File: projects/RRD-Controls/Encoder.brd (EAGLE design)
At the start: 20.3 x 35.6 mm, 3 parts

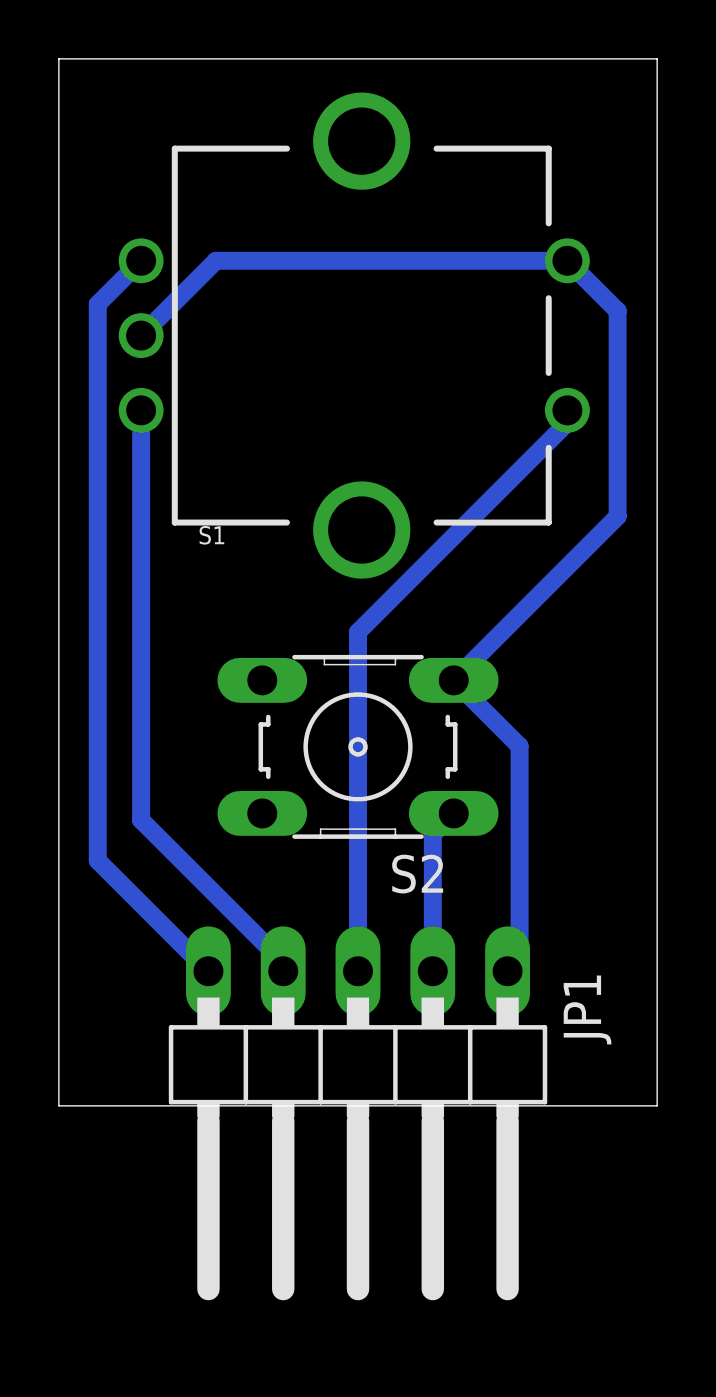
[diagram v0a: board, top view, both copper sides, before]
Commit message: New 32-bit AMR3350 (probably will be renamed), + other edits
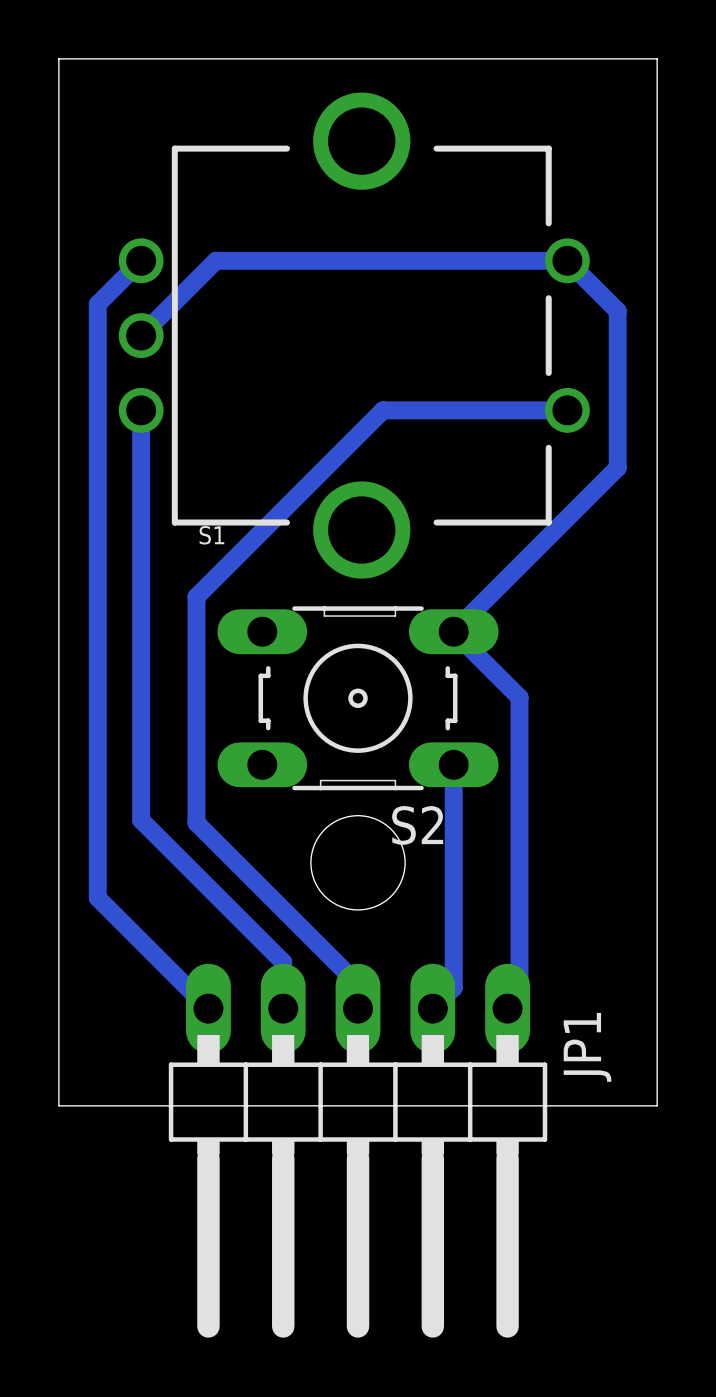
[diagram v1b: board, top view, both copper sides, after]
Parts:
- moved S2 1.65 mm to (10.2, 13.8)
- moved JP1 1.27 mm to (10.2, -0.51)
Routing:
- net ENC_SW: track 22.0 -> 31.5 mm
- net RESET: track 5.65 -> 8.57 mm
- net GND: track 43.8 -> 45.0 mm
- net ENC_B: track 21.0 -> 22.3 mm
- net ENC_A: track 26.3 -> 27.6 mm
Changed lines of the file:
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@@
 <setting verticaltext="up"/>
 </settings>
-<grid distance="50" unitdist="mil" unit="mil" style="dots" multiple="1" display="yes" altdistance="5" altunitdist="mil" altunit="mil"/>
+<grid distance="50" unitdist="mil" unit="mm" style="dots" multiple="1" display="yes" altdistance="5" altunitdist="mil" altunit="mil"/>
 <layers>
 <layer number="1" name="Top" color="4" fill="1" visible="yes" active="yes"/>
@@
 <layer number="43" name="vRestrict" color="2" fill="10" visible="yes" active="yes"/>
 <layer number="44" name="Drills" color="7" fill="1" visible="no" active="yes"/>
-<layer number="45" name="Holes" color="7" fill="1" visible="no" active="yes"/>
+<layer number="45" name="Holes" color="7" fill="1" visible="yes" active="yes"/>
 <layer number="46" name="Milling" color="3" fill="1" visible="no" active="yes"/>
 <layer number="47" name="Measures" color="7" fill="1" visible="no" active="yes"/>
@@
 </layers>
 <board>
+<fusionsync huburn="a.cGVyc29uYWw6dWUyYWY5YmU0" projecturn="a.cGVyc29uYWw6dWUyYWY5YmU0IzIwMTgwNTA2MTMwNzk4NzU2" f3durn="urn:adsk.wipprod:dm.lineage:ghSnY2K8RTWHbbuxzUc_hQ" pcbguid="3d89ad0b-1789-465d-8edf-d24fb5f6a05f" lastpulledtime="" lastsyncedchangeguid="ebffb4b7-4351-7158-2c67-7c1263c4be28"/>
 <plain>
 <wire x1="0" y1="0" x2="20.32" y2="0" width="0" layer="20"/>
@@
 <wire x1="20.32" y1="35.56" x2="0" y2="35.56" width="0" layer="20"/>
 <wire x1="0" y1="35.56" x2="0" y2="0" width="0" layer="20"/>
+<hole x="10.16" y="8.255" drill="3.2"/>
 </plain>
 <attributes>
@@
 </autorouter>
 <elements>
-<element name="JP1" library="pinhead" library_urn="urn:adsk.eagle:library:325" package="1X05/90" package3d_urn="urn:adsk.eagle:package:22467/2" value="" x="10.16" y="0.762" smashed="yes" rot="R180">
-<attribute name="NAME" x="17.145" y="4.572" size="1.27" layer="25" ratio="10" rot="R270"/>
-<attribute name="VALUE" x="1.905" y="4.572" size="1.27" layer="27" rot="R270"/>
+<element name="JP1" library="pinhead" library_urn="urn:adsk.eagle:library:325" package="1X05/90" package3d_urn="urn:adsk.eagle:package:22467/2" value="" x="10.16" y="-0.508" smashed="yes" rot="R180">
+<attribute name="NAME" x="17.145" y="3.302" size="1.27" layer="25" ratio="10" rot="R270"/>
+<attribute name="VALUE" x="1.905" y="3.302" size="1.27" layer="27" rot="R270"/>
 </element>
 <element name="S1" library="SparkFun-Switches" library_urn="urn:adsk.eagle:library:535" package="ROTARY_ENC_PLAIN" package3d_urn="urn:adsk.eagle:package:40158/1" value="ENCODER-SWITCH" x="10.287" y="26.162" smashed="yes" rot="R180">
@@
 <attribute name="VALUE" x="5.207" y="32.639" size="0.6096" layer="27" font="vector" ratio="20" rot="R180" align="top-center"/>
 </element>
-<element name="S2" library="switch-omron" library_urn="urn:adsk.eagle:library:377" package="B3F-10XX" package3d_urn="urn:adsk.eagle:package:27496/1" value="" x="10.16" y="12.192" smashed="yes" rot="R180">
-<attribute name="MF" value="" x="-7.62" y="46.482" size="1.778" layer="27" rot="R180" display="off"/>
-<attribute name="MPN" value="B3F-1000" x="-7.62" y="46.482" size="1.778" layer="27" rot="R180" display="off"/>
-<attribute name="NAME" x="13.208" y="8.509" size="1.27" layer="25" ratio="10" rot="R180"/>
-<attribute name="OC_FARNELL" value="176432" x="-7.62" y="46.482" size="1.778" layer="27" rot="R180" display="off"/>
-<attribute name="OC_NEWARK" value="36M3542" x="-7.62" y="46.482" size="1.778" layer="27" rot="R180" display="off"/>
-<attribute name="VALUE" x="13.208" y="17.272" size="1.27" layer="27" ratio="10" rot="R180"/>
+<element name="S2" library="switch-omron" library_urn="urn:adsk.eagle:library:377" package="B3F-10XX" package3d_urn="urn:adsk.eagle:package:27496/1" value="" x="10.16" y="13.843" smashed="yes" rot="R180">
+<attribute name="MF" value="" x="-7.62" y="48.133" size="1.778" layer="27" rot="R180" display="off"/>
+<attribute name="MPN" value="B3F-1000" x="-7.62" y="48.133" size="1.778" layer="27" rot="R180" display="off"/>
+<attribute name="NAME" x="13.208" y="10.16" size="1.27" layer="25" ratio="10" rot="R180"/>
+<attribute name="OC_FARNELL" value="176432" x="-7.62" y="48.133" size="1.778" layer="27" rot="R180" display="off"/>
+<attribute name="OC_NEWARK" value="36M3542" x="-7.62" y="48.133" size="1.778" layer="27" rot="R180" display="off"/>
+<attribute name="VALUE" x="13.208" y="18.923" size="1.27" layer="27" ratio="10" rot="R180"/>
 </element>
 </elements>
@@
 <wire x1="2.794" y1="26.162" x2="5.334" y2="28.702" width="0.6096" layer="16"/>
 <wire x1="17.272" y1="28.702" x2="18.9792" y2="26.9948" width="0.6096" layer="16"/>
-<wire x1="18.9792" y1="20.0206" x2="13.4112" y2="14.4526" width="0.6096" layer="16"/>
-<wire x1="18.9792" y1="26.9948" x2="18.9792" y2="20.0206" width="0.6096" layer="16"/>
-<wire x1="15.6464" y1="12.2174" x2="15.6464" y2="4.9784" width="0.6096" layer="16"/>
-<wire x1="15.6464" y1="4.9784" x2="15.24" y2="4.572" width="0.6096" layer="16"/>
-<wire x1="13.4112" y1="14.4526" x2="15.6464" y2="12.2174" width="0.6096" layer="16"/>
+<wire x1="18.9792" y1="21.6716" x2="13.4112" y2="16.1036" width="0.6096" layer="16"/>
+<wire x1="18.9792" y1="26.9948" x2="18.9792" y2="21.6716" width="0.6096" layer="16"/>
+<wire x1="15.6464" y1="13.8684" x2="15.6464" y2="3.7084" width="0.6096" layer="16"/>
+<wire x1="15.6464" y1="3.7084" x2="15.24" y2="3.302" width="0.6096" layer="16"/>
+<wire x1="13.4112" y1="16.1036" x2="15.6464" y2="13.8684" width="0.6096" layer="16"/>
 </signal>
 <signal name="RESET">
 <contactref element="S2" pad="1"/>
 <contactref element="JP1" pad="2"/>
-<wire x1="12.7" y1="4.572" x2="12.7" y2="9.2202" width="0.6096" layer="16"/>
-<wire x1="12.7" y1="9.2202" x2="13.4112" y2="9.9314" width="0.6096" layer="16"/>
+<wire x1="13.4112" y1="11.5824" x2="13.4112" y2="4.0132" width="0.6096" layer="16"/>
+<wire x1="13.4112" y1="4.0132" x2="12.7" y2="3.302" width="0.6096" layer="16"/>
 </signal>
 <signal name="ENC_A">
@@
 <contactref element="JP1" pad="5"/>
 <wire x1="2.794" y1="28.702" x2="1.3208" y2="27.2288" width="0.6096" layer="16"/>
-<wire x1="1.3208" y1="8.3312" x2="5.08" y2="4.572" width="0.6096" layer="16"/>
-<wire x1="1.3208" y1="27.2288" x2="1.3208" y2="8.3312" width="0.6096" layer="16"/>
+<wire x1="1.3208" y1="7.0612" x2="5.08" y2="3.302" width="0.6096" layer="16"/>
+<wire x1="1.3208" y1="27.2288" x2="1.3208" y2="7.0612" width="0.6096" layer="16"/>
 </signal>
 <signal name="ENC_B">
@@
 <contactref element="JP1" pad="4"/>
 <wire x1="2.794" y1="23.622" x2="2.794" y2="9.703425" width="0.6096" layer="16"/>
-<wire x1="7.62" y1="4.572" x2="7.62" y2="4.877425" width="0.6096" layer="16"/>
+<wire x1="7.62" y1="3.302" x2="7.62" y2="4.877425" width="0.6096" layer="16"/>
 <wire x1="7.62" y1="4.877425" x2="2.794" y2="9.703425" width="0.6096" layer="16"/>
 </signal>
@@
 <contactref element="S1" pad="SW+"/>
 <contactref element="JP1" pad="3"/>
-<wire x1="17.272" y1="23.622" x2="17.272" y2="23.20234375" width="0.6096" layer="16"/>
-<wire x1="17.272" y1="23.20234375" x2="10.16" y2="16.09034375" width="0.6096" layer="16"/>
-<wire x1="10.16" y1="16.09034375" x2="10.16" y2="4.572" width="0.6096" layer="16"/>
+<wire x1="10.16" y1="3.302" x2="10.16" y2="4.1243625" width="0.6096" layer="16"/>
+<wire x1="10.16" y1="4.1243625" x2="4.6736" y2="9.6107625" width="0.6096" layer="16"/>
+<wire x1="4.6736" y1="9.6107625" x2="4.6736" y2="17.28525625" width="0.6096" layer="16"/>
+<wire x1="11.01034375" y1="23.622" x2="17.272" y2="23.622" width="0.6096" layer="16"/>
+<wire x1="4.6736" y1="17.28525625" x2="11.01034375" y2="23.622" width="0.6096" layer="16"/>
 </signal>
 </signals>
@@
 </note>
 <note version="8.3" severity="warning">
+Since Version 8.3, EAGLE supports Fusion synchronisation.
+This feature will not be available in this version and saving
+the document will break the link to the Fusion PCB feature.
+</note>
+<note version="8.3" severity="warning">
